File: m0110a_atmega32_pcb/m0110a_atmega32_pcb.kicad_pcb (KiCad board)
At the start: 2 copper layers, 17.8 x 51.6 mm, 5 parts, among them J1 Conn_01x40_Pin, J2 ISP, J3 Serial, U2 ATmega32A-M

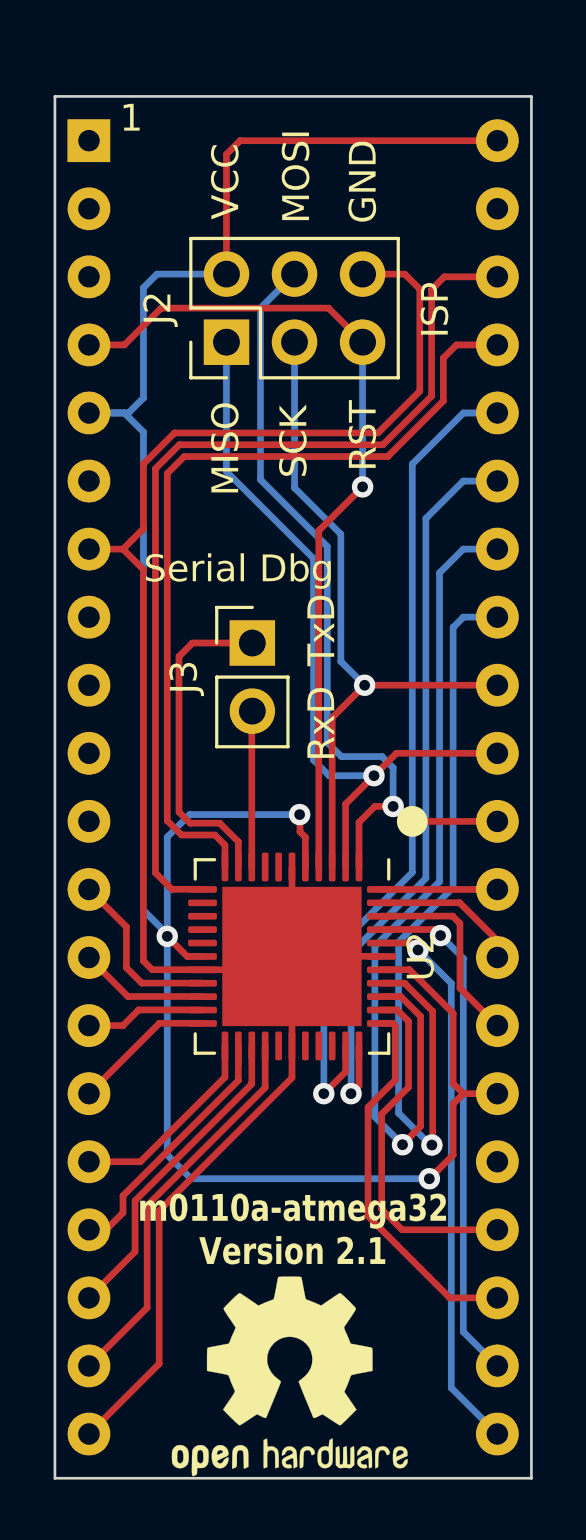
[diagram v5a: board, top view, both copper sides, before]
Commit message: Updated PCBs
- Increased hole size on 40 pin connector to accomodate standard pin headers
- Moved ISP connector on SMD board to clear support under spacebar
- Improved labeling on thru-hole board for ISP connector
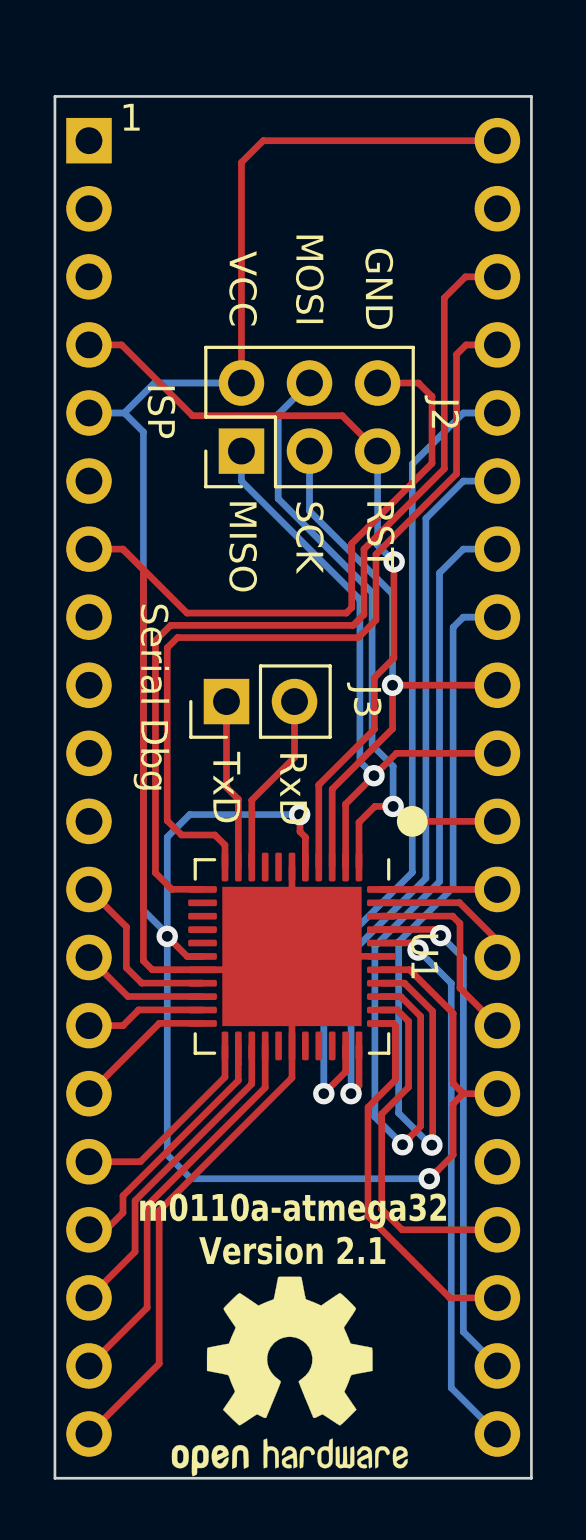
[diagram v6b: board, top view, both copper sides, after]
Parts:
- moved J2 4.10 mm to (149.2, 78.9)
- moved J3 2.39 mm to (148.6, 88.2), turned to 90 degrees
- renumbered U2 to U1
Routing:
- net /TXD: track 12.4 -> 6.35 mm
- net /ROW5: track 30.6 -> 25.4 mm
- net /ROW6: track 28.2 -> 23.7 mm
- net /ROW7: track 26.8 -> 22.3 mm
- net RESET: track 31.6 -> 29.3 mm
- net +5V: track 88.9 -> 87.4 mm
- net /RXD: track 5.82 -> 6.83 mm
- net /KB_DATA: track 35.1 -> 34.2 mm
- net /KB_CLK: track 31.5 -> 30.8 mm
